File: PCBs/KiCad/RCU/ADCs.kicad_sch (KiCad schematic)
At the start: 18 parts, among them U600 ADC121C027CIMK/NOPB, U601 OPA320, U602 ADC121C027CIMK/NOPB, U603 OPA320

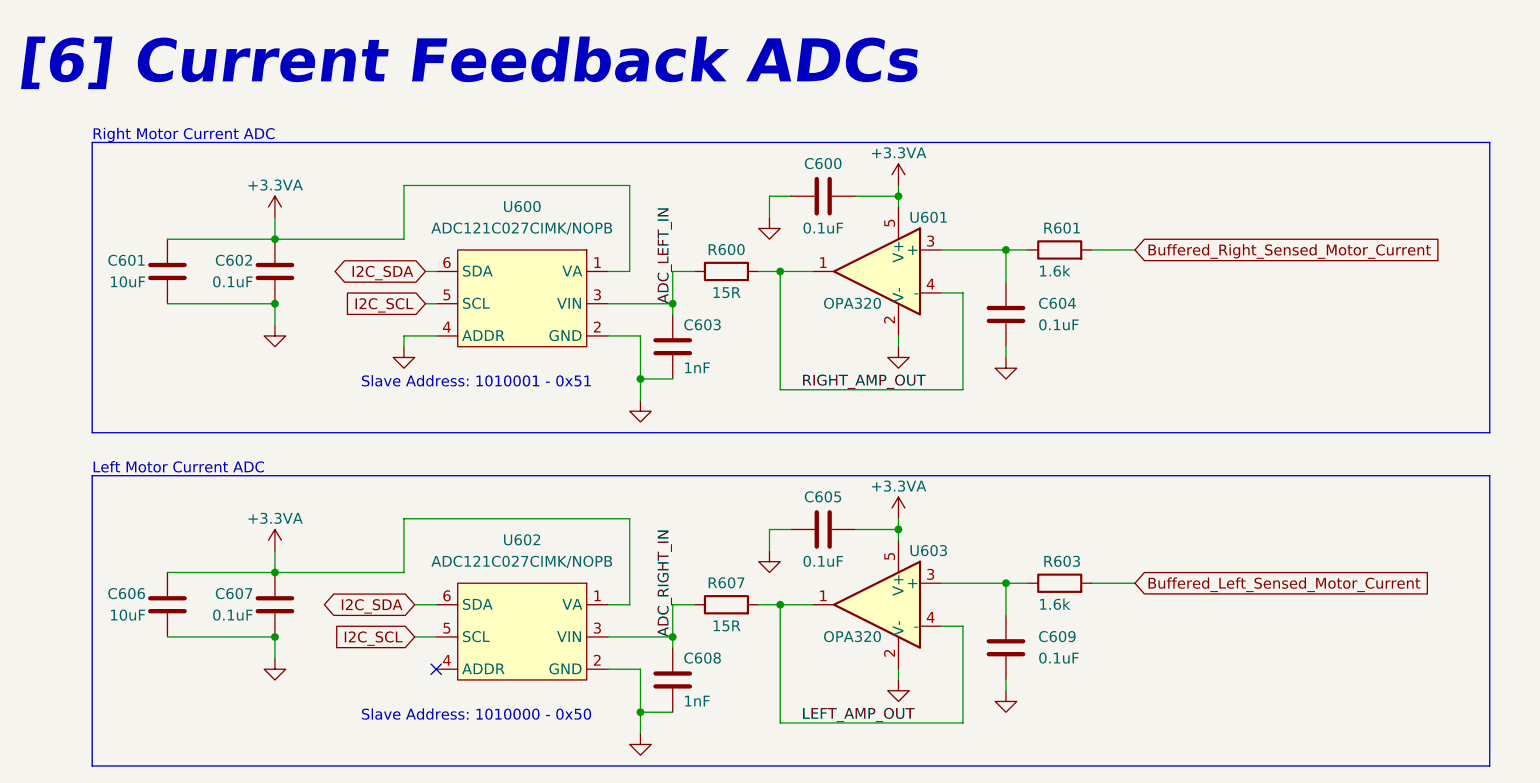
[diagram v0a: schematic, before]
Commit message: Moved project library one folder up to Kicad Folder
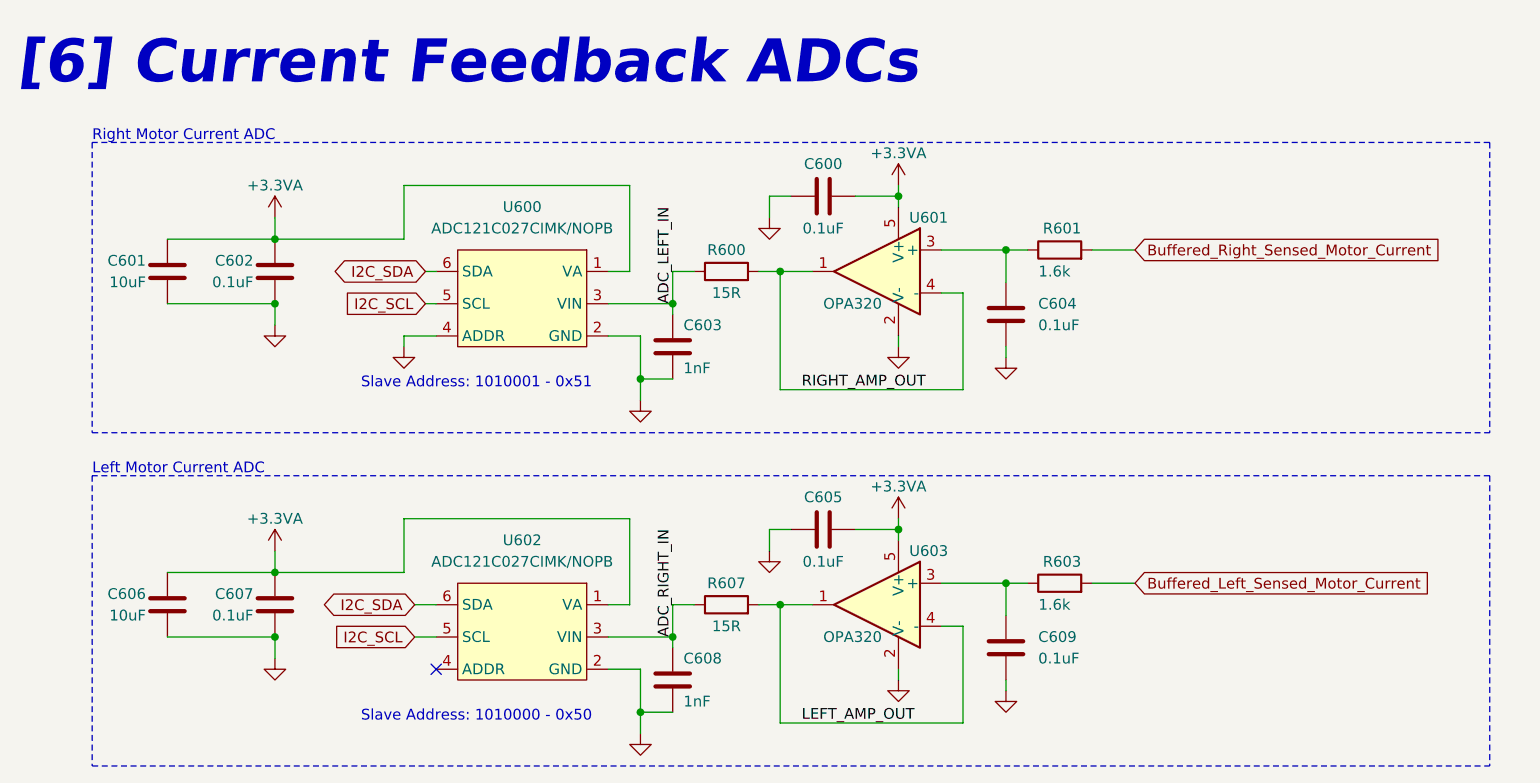
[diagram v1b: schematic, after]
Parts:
- U600, U602: symbol Ghanis_Symbols_KiCad6:ADC121C027CIMK/NOPB -> Ghanis_Symbols_KiCad6:ADC121C027CIMK/NOPB
